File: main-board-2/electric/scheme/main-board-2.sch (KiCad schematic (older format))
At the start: 125 parts, among them K1 power-switch, K2 usb-power-switch, P1 batt, P10 screw-3, P11 screw-1, P12 screw-4, P13 screw-2, P14 gpio-big, P15 gpio-small, P16 moto-1, P17 moto-2, P2 CONN_4, P3 trigger-btn, P4 CONN_3X2, P5 reg-short-to-gnd-1, P6 reg-short-to-gnd-2, P7 bootloader, P8 cross board conn, P9 rst, Q1 IRLML2244, Q10 IRLML2244, Q11 sot223, Q12 bc857, Q13 irlml2244, Q2 BC847, Q3 IRLML2244, Q4 IRLML2244, Q5 BC847, Q6 BC847, Q7 BC847, Q8 BC847, Q9 IRLML2244, U1 LM317AEMP, U2 LM317AT, U3 LM317AEMP, U4 LM317AT, U5 LM293, U6 L298, U7 MINI-USB-B, X1 8MHz

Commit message: Placing elements...
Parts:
- added R7: 30k, symbol R
- R46: renamed from R45; value 9 -> 3
- R47: renamed from R46; value 9 -> 3
- renumbered C6 to C4, C4 to C5, C5 to C6, R9 to R10, R10 to R11, R11 to R12, R12 to R13, R13 to R14, R14 to R15, R15 to R16, R16 to R17, R17 to R18, R18 to R19, R19 to R20, R20 to R21, R21 to R22, R22 to R23, R23 to R24, R24 to R25, R25 to R26, R26 to R27, R27 to R28, R28 to R29, R29 to R30, R30 to R31, R31 to R32, R32 to R33, R33 to R34, R34 to R35, R35 to R36, R36 to R37, R37 to R38, R38 to R39, R39 to R40, R40 to R41, R41 to R42, R42 to R43, R43 to R44, R44 to R45, R47 to R48, R48 to R49, R7 to R8, R8 to R9
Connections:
- wire segments 421 -> 422
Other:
- moved on the sheet: C4

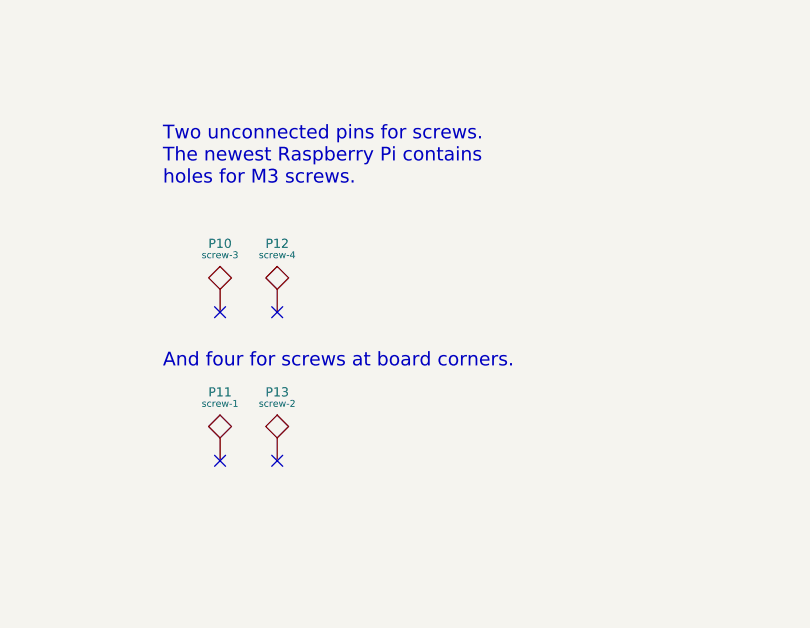
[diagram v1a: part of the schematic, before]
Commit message: Removed unused screw holes.
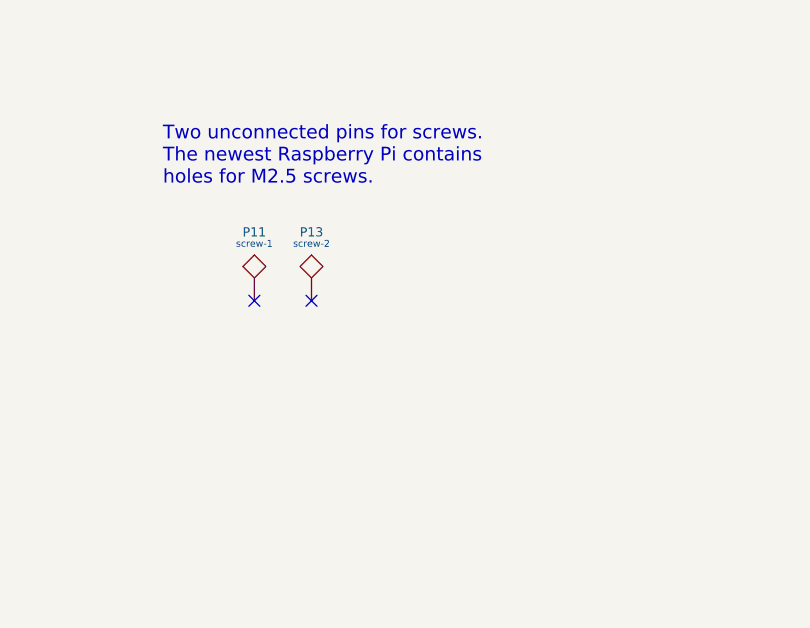
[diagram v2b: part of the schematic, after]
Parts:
- removed P10: screw-3, ~, symbol TST
- removed P12: screw-4, ~, symbol TST
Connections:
- no-connect marks 9 -> 7
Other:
- note added: "Two unconnected pins for screws.\nThe newest Raspberry Pi contains \nholes for M2.5 screws."
- note removed: "And four for screws at board corners."
- note removed: "Two unconnected pins for screws.\nThe newest Raspberry Pi contains \nholes for M3 screws."
- moved on the sheet: P11, P13
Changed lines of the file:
@@
 Text Notes 8850 17150 0    60   ~ 0
 Cross board communication socket.\nThere is one at this board. But there should \nbe two neighbour such sockets on all other \nboards to be able to stack them together.
-$Comp
-L TST P10
-U 1 1 52A0D55D
-P 11550 13350
-F 0 "P10" H 11550 13650 40  0000 C CNN
-F 1 "screw-3" H 11550 13600 30  0000 C CNN
-F 2 "~" H 11550 13350 60  0000 C CNN
-F 3 "~" H 11550 13350 60  0000 C CNN
-	1    11550 13350
-	1    0    0    -1
-$EndComp
-NoConn ~ 11550 13350
-$Comp
-L TST P12
-U 1 1 52A0D564
-P 11800 13350
-F 0 "P12" H 11800 13650 40  0000 C CNN
-F 1 "screw-4" H 11800 13600 30  0000 C CNN
-F 2 "~" H 11800 13350 60  0000 C CNN
-F 3 "~" H 11800 13350 60  0000 C CNN
-	1    11800 13350
-	1    0    0    -1
-$EndComp
-NoConn ~ 11800 13350
 Text Notes 11300 12800 0    60   ~ 0
-Two unconnected pins for screws.\nThe newest Raspberry Pi contains \nholes for M3 screws.
+Two unconnected pins for screws.\nThe newest Raspberry Pi contains \nholes for M2.5 screws.
 $Comp
 L CONN_4 P2
@@
 L TST P11
 U 1 1 52A0D5BE
-P 11550 14000
-F 0 "P11" H 11550 14300 40  0000 C CNN
-F 1 "screw-1" H 11550 14250 30  0000 C CNN
-F 2 "~" H 11550 14000 60  0000 C CNN
-F 3 "~" H 11550 14000 60  0000 C CNN
-	1    11550 14000
+P 11700 13300
+F 0 "P11" H 11700 13600 40  0000 C CNN
+F 1 "screw-1" H 11700 13550 30  0000 C CNN
+F 2 "~" H 11700 13300 60  0000 C CNN
+F 3 "~" H 11700 13300 60  0000 C CNN
+	1    11700 13300
 	1    0    0    -1
 $EndComp
-NoConn ~ 11550 14000
-Text Notes 11300 13600 0    60   ~ 0
-And four for screws at board corners.
+NoConn ~ 11700 13300
 $Comp
 L C C10
@@
 L TST P13
 U 1 1 52A0E1AF
-P 11800 14000
-F 0 "P13" H 11800 14300 40  0000 C CNN
-F 1 "screw-2" H 11800 14250 30  0000 C CNN
-F 2 "~" H 11800 14000 60  0000 C CNN
-F 3 "~" H 11800 14000 60  0000 C CNN
-	1    11800 14000
+P 11950 13300
+F 0 "P13" H 11950 13600 40  0000 C CNN
+F 1 "screw-2" H 11950 13550 30  0000 C CNN
+F 2 "~" H 11950 13300 60  0000 C CNN
+F 3 "~" H 11950 13300 60  0000 C CNN
+	1    11950 13300
 	1    0    0    -1
 $EndComp
-NoConn ~ 11800 14000
+NoConn ~ 11950 13300
 $Comp
 L CONN_2 P7

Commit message: Routing...
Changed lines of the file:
@@
 Text Label 8850 7350 0    60   ~ 0
 in-moto3
-Text Label 14400 8850 0    60   ~ 0
+Text Label 14400 9850 0    60   ~ 0
 in-moto2
-Text Label 14400 9050 0    60   ~ 0
+Text Label 14400 10050 0    60   ~ 0
 in-moto1
 Text Label 14550 3050 0    60   ~ 0
@@
 	0    -1   -1   0
 $EndComp
-Text Label 14400 9850 0    60   ~ 0
+Text Label 14400 9050 0    60   ~ 0
 led1
 Text Label 14400 9450 0    60   ~ 0
@@
 Wire Wire Line
 	9500 7350 8800 7350
-Text Label 14400 10050 0    60   ~ 0
+Text Label 14400 8850 0    60   ~ 0
 led2
 Text Label 14850 5550 0    60   ~ 0

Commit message: Routing...
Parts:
- added P10: rst, ~, symbol TST
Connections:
- wire segments 422 -> 423
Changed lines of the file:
@@
 	4950 4650 4950 4350
 Connection ~ 4950 4350
+$Comp
+L TST P10
+U 1 1 52A4BFA0
+P 8650 4050
+F 0 "P10" H 8650 4350 40  0000 C CNN
+F 1 "rst" H 8650 4300 30  0000 C CNN
+F 2 "~" H 8650 4050 60  0000 C CNN
+F 3 "~" H 8650 4050 60  0000 C CNN
+	1    8650 4050
+	1    0    0    -1
+$EndComp
+Wire Wire Line
+	8650 4050 8650 4250
+Connection ~ 8650 4250
 $EndSCHEMATC

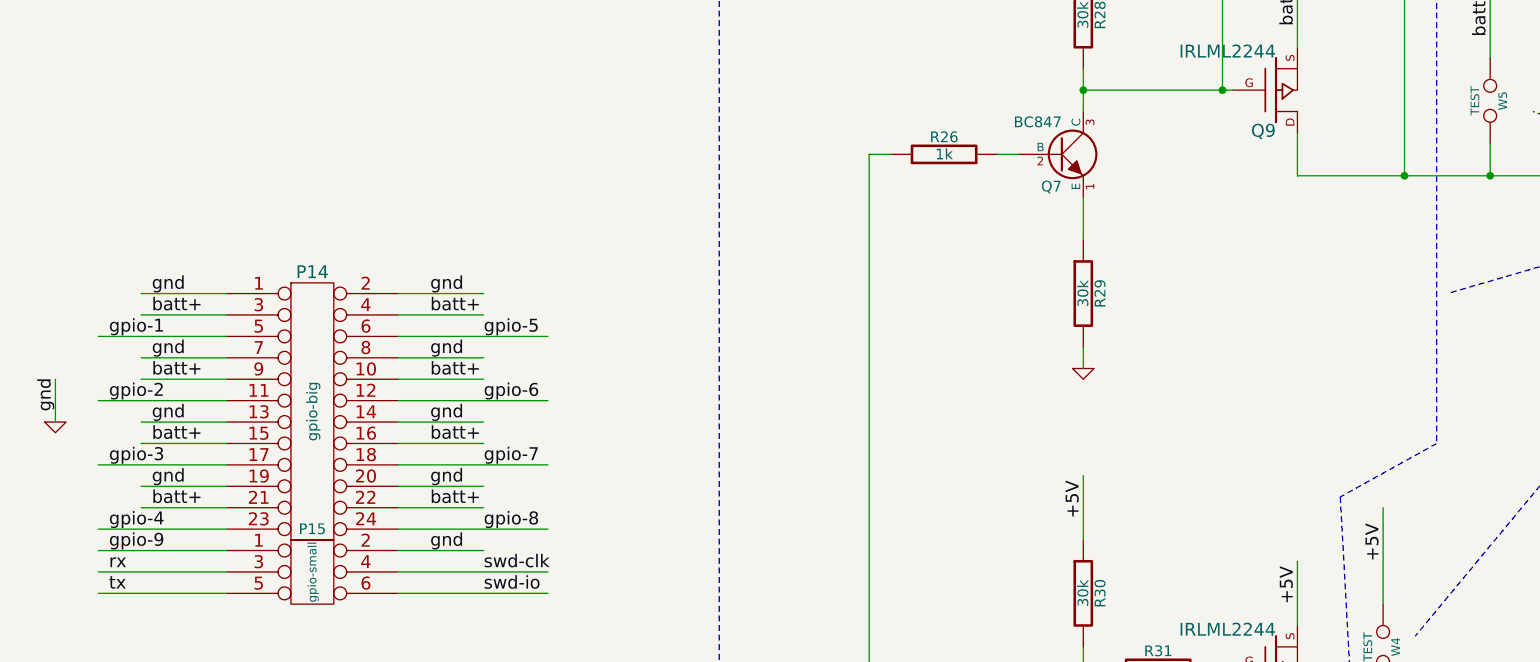
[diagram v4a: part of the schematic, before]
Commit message: Routing. Made servo power switchable.
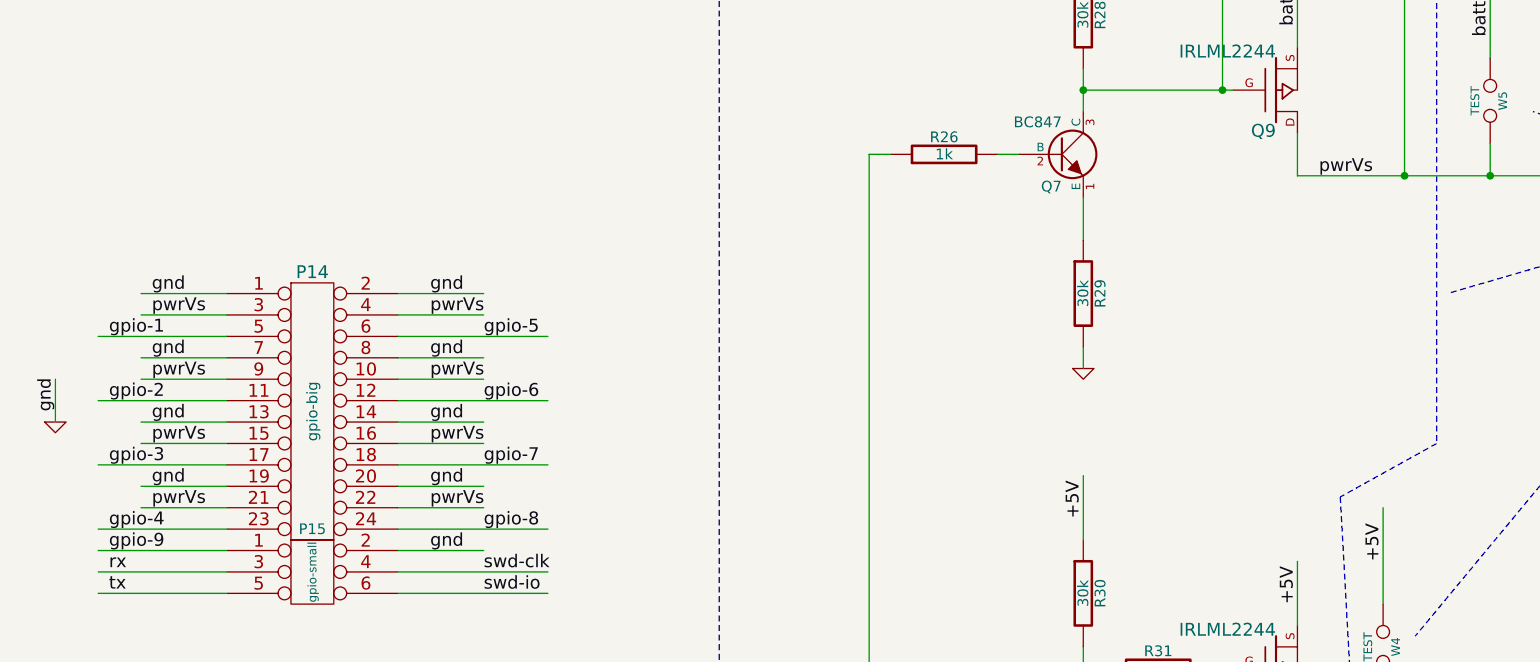
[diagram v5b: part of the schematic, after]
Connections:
- net labels added: pwrVs
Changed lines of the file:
@@
 Sheet 1 1
 Title "Main board 2"
-Date "8 dec 2013"
+Date "9 dec 2013"
 Rev ""
 Comp ""
@@
 Text Label 16350 4000 0    60   ~ 0
 gnd
-Text Label 16350 3200 0    60   ~ 0
-batt+
-Text Label 16350 3500 0    60   ~ 0
-batt+
-Text Label 16350 3800 0    60   ~ 0
-batt+
-Text Label 16350 4100 0    60   ~ 0
-batt+
 Wire Wire Line
 	17500 3100 17900 3100
@@
 Text Label 17650 4000 0    60   ~ 0
 gnd
-Text Label 17650 3200 0    60   ~ 0
-batt+
-Text Label 17650 3500 0    60   ~ 0
-batt+
-Text Label 17650 3800 0    60   ~ 0
-batt+
-Text Label 17650 4100 0    60   ~ 0
-batt+
 Text Label 14600 3350 0    60   ~ 0
 gpio-1
@@
 	8650 4050 8650 4250
 Connection ~ 8650 4250
+Text Label 21800 2550 0    60   ~ 0
+pwrVs
+Text Label 16350 3200 0    60   ~ 0
+pwrVs
+Text Label 16350 3500 0    60   ~ 0
+pwrVs
+Text Label 16350 3800 0    60   ~ 0
+pwrVs
+Text Label 16350 4100 0    60   ~ 0
+pwrVs
+Text Label 17650 3200 0    60   ~ 0
+pwrVs
+Text Label 17650 3500 0    60   ~ 0
+pwrVs
+Text Label 17650 3800 0    60   ~ 0
+pwrVs
+Text Label 17650 4100 0    60   ~ 0
+pwrVs
 $EndSCHEMATC

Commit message: Routing...
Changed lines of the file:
@@
 	1    0    0    -1
 $EndComp
+Text Label 8850 7350 0    60   ~ 0
+in-moto4
 Text Label 8850 6650 0    60   ~ 0
-in-moto4
-Text Label 8850 7350 0    60   ~ 0
 in-moto3
 Text Label 14400 9850 0    60   ~ 0

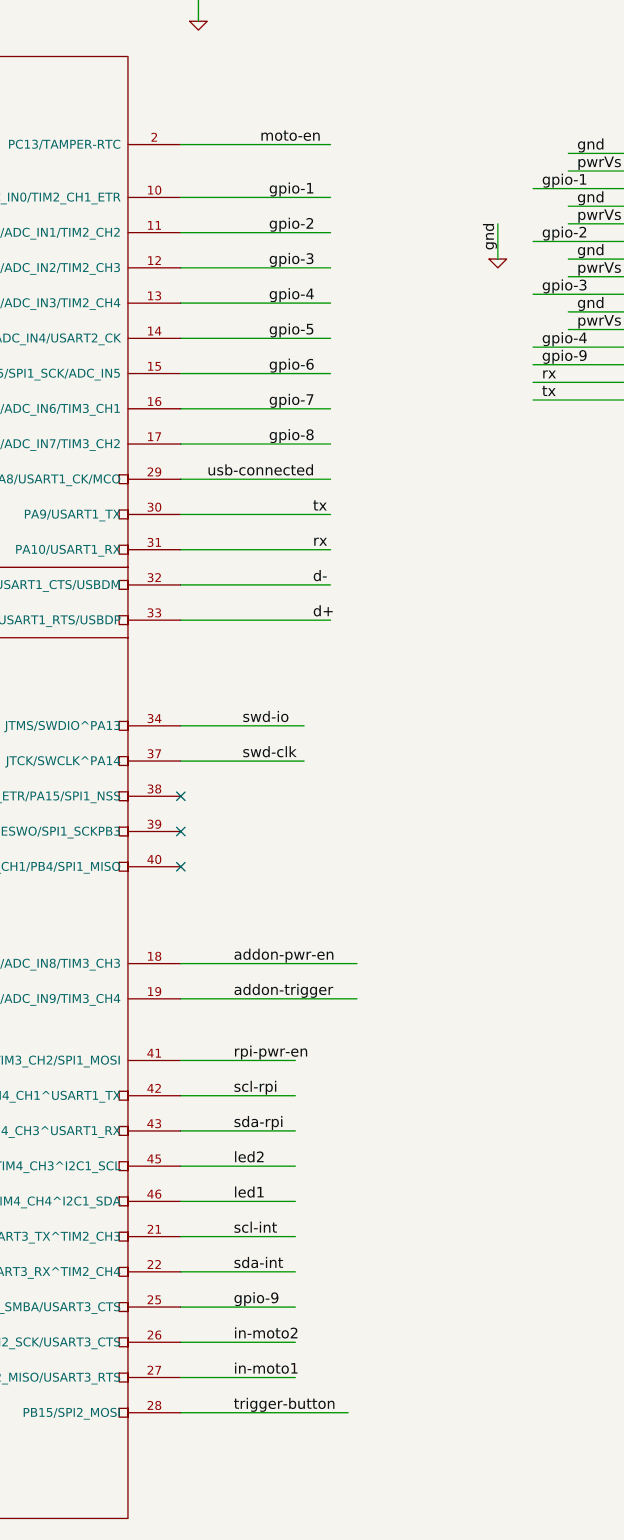
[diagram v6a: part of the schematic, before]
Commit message: Routing rx and tx...
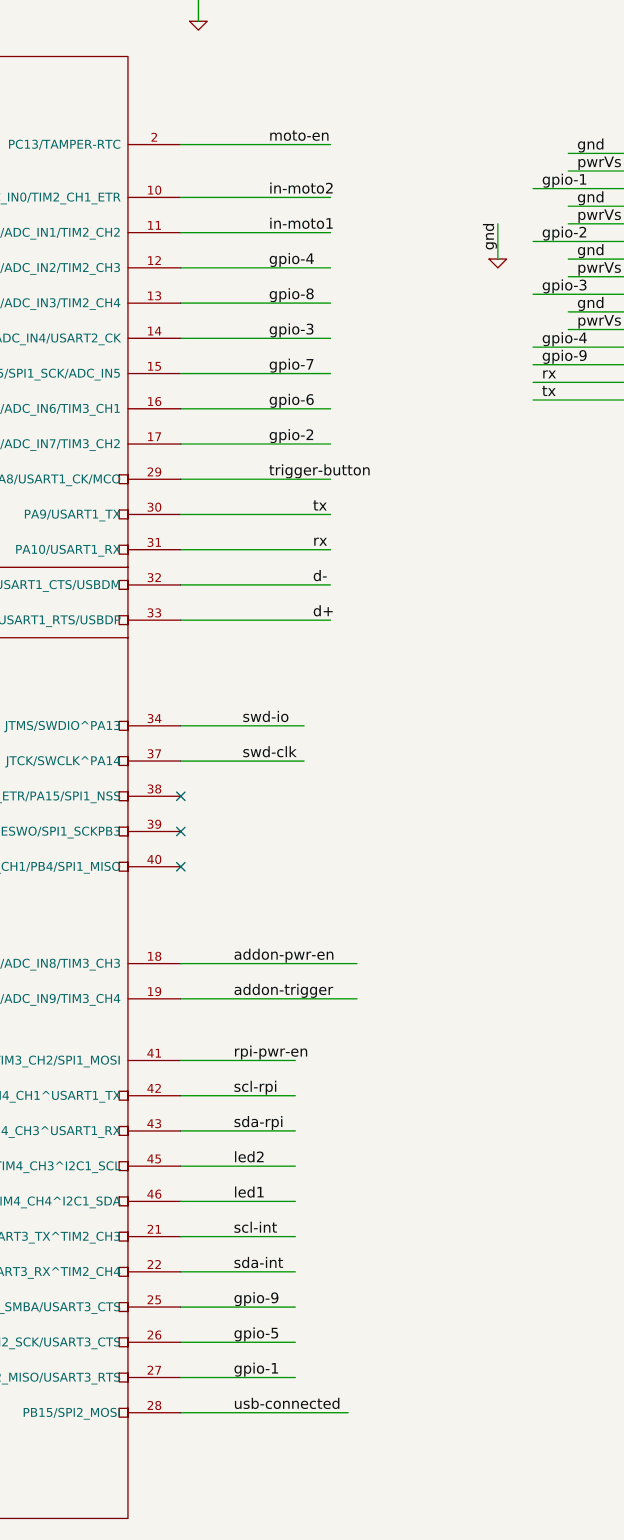
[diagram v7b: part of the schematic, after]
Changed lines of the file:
@@
 Text Label 8850 6650 0    60   ~ 0
 in-moto3
-Text Label 14400 9850 0    60   ~ 0
+Text Label 14600 3350 0    60   ~ 0
 in-moto2
-Text Label 14400 10050 0    60   ~ 0
+Text Label 14600 3550 0    60   ~ 0
 in-moto1
-Text Label 14550 3050 0    60   ~ 0
+Text Label 14600 3050 0    60   ~ 0
 moto-en
 Text Label 19250 5150 0    60   ~ 0
@@
 	1    0    0    1
 $EndComp
-Text Label 14400 10250 0    60   ~ 0
+Text Label 14600 4950 0    60   ~ 0
 trigger-button
 $Comp
@@
 	24800 19500 24800 19400
 Connection ~ 24800 19500
-Text Label 14250 4950 0    60   ~ 0
+Text Label 14400 10250 0    60   ~ 0
 usb-connected
 Text Notes 4750 6350 2    60   ~ 0
@@
 Text Label 17650 4000 0    60   ~ 0
 gnd
-Text Label 14600 3350 0    60   ~ 0
+Text Label 14400 10050 0    60   ~ 0
 gpio-1
-Text Label 14600 3550 0    60   ~ 0
+Text Label 14600 4750 0    60   ~ 0
 gpio-2
-Text Label 14600 3750 0    60   ~ 0
+Text Label 14600 4150 0    60   ~ 0
 gpio-3
-Text Label 14600 3950 0    60   ~ 0
+Text Label 14600 3750 0    60   ~ 0
 gpio-4
-Text Label 14600 4150 0    60   ~ 0
+Text Label 14400 9850 0    60   ~ 0
 gpio-5
-Text Label 14600 4350 0    60   ~ 0
-gpio-6
 Text Label 14600 4550 0    60   ~ 0
+gpio-6
+Text Label 14600 4350 0    60   ~ 0
 gpio-7
-Text Label 14600 4750 0    60   ~ 0
+Text Label 14600 3950 0    60   ~ 0
 gpio-8
 Text Label 16150 3300 0    60   ~ 0

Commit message: Routing...
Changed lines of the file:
@@
 Text Label 3250 13600 0    60   ~ 0
 trigger-button
-Text Label 14400 7700 0    60   ~ 0
+Text Label 14400 9850 0    60   ~ 0
 addon-pwr-en
 $Comp
@@
 Text Label 17650 4000 0    60   ~ 0
 gnd
-Text Label 14400 10050 0    60   ~ 0
+Text Label 14400 7700 0    60   ~ 0
 gpio-1
 Text Label 14600 4750 0    60   ~ 0
@@
 Text Label 14600 3750 0    60   ~ 0
 gpio-4
-Text Label 14400 9850 0    60   ~ 0
+Text Label 14400 10050 0    60   ~ 0
 gpio-5
 Text Label 14600 4550 0    60   ~ 0
